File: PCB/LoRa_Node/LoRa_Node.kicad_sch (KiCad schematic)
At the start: 76 parts, among them IC1 SPX5205M5-L/TR, J1 Conn_01x04_Socket, J2 Conn_01x02_Pin, J3 UF.L, J4 2x5_2.00mm, J6 Conn_01x06_Socket, J7 Conn_01x03_Socket, Q1 AO3401A, SW1 SW_SPST, U1 BME280, U2 RFM95W-868S2, U3 STM32L151C8T6, U4 SIM800L-CORE, U5 SX1308, Y1 12MHz, Y2 32.768kHz

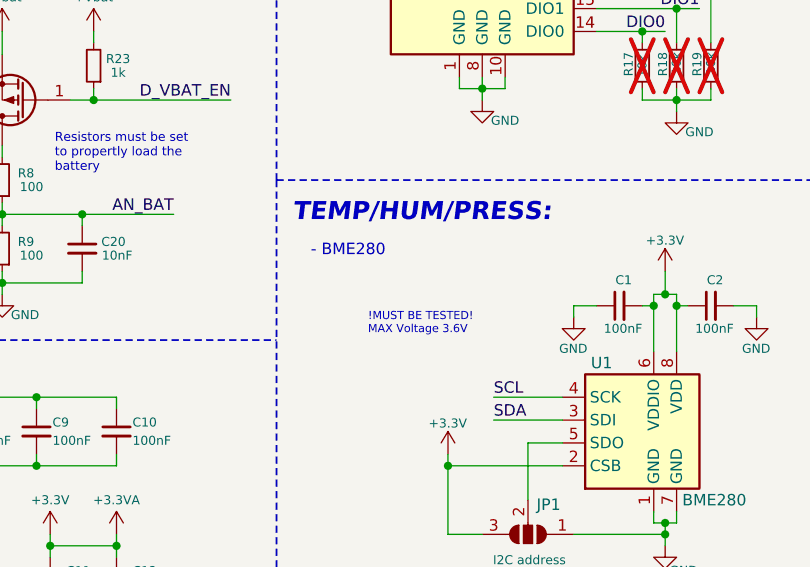
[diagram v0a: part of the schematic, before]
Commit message: Bugfix
solved problem with LoRa packet counter (flash write error after sleep)
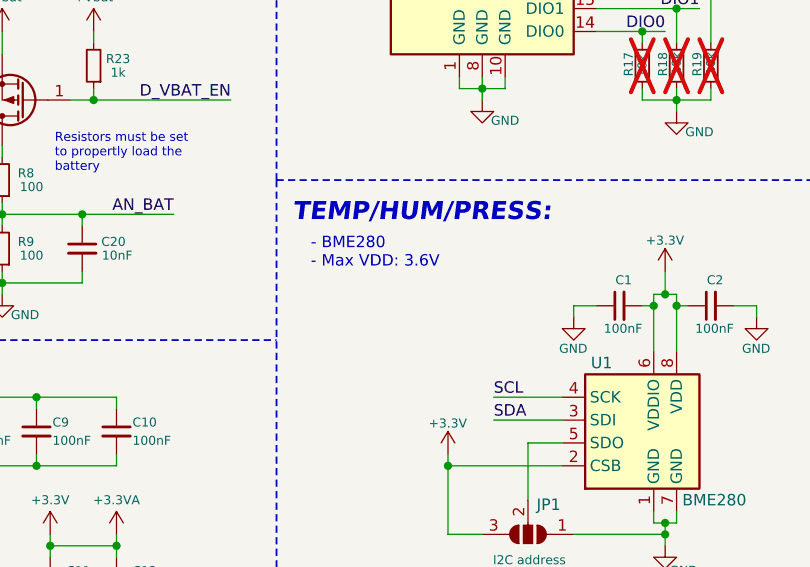
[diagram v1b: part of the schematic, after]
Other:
- note added: "- BME280 - Max VDD: 3.6V"
- note removed: "!MUST BE TESTED! MAX Voltage 3.6V"
- note removed: "- BME280"
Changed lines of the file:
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@@
 		)
 	)
-	(text "- BME280"
+	(text "- BME280\n- Max VDD: 3.6V"
 		(exclude_from_sim no)
-		(at 161.29 87.376 0)
+		(at 161.29 88.646 0)
 		(effects
 			(font
@@
 		)
 	)
-	(text "!MUST BE TESTED!\nMAX Voltage 3.6V"
-		(exclude_from_sim no)
-		(at 167.64 94.742 0)
-		(effects
-			(font
-				(size 0.9 0.9)
-				(color 255 0 0 1)
-			)
-			(justify left)
-		)
-	)
